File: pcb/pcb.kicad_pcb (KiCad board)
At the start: 2 copper layers, 347.8 x 133.5 mm, 250 parts, among them J1 USB_C_Receptacle_USB2.0_16P, SW1 SW_Push, U1 USBLC6-2SC6, U2 XC6206PxxxMR, U3 STM32F072CBTx

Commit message: Matrix ready
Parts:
- moved D10 9.62 mm to (226.1, 47.0), turned to 90 degrees
- moved D13 9.62 mm to (283.2, 47.0), turned to 90 degrees
- moved D14 9.62 mm to (302.3, 47.0), turned to 90 degrees
- moved D5 9.62 mm to (130.8, 47.0), turned to 90 degrees
- moved D7 9.62 mm to (168.9, 47.0), turned to 90 degrees
- moved D8 9.62 mm to (188.0, 47.0), turned to 90 degrees
- moved D9 9.62 mm to (207.0, 47.0), turned to 90 degrees
- moved D4 9.62 mm to (111.8, 47.0), turned to 90 degrees
- moved D11 9.62 mm to (245.1, 47.0), turned to 90 degrees
- moved D6 9.62 mm to (149.9, 47.0), turned to 90 degrees
- moved D12 9.62 mm to (264.2, 47.0), turned to 90 degrees
- moved D45 9.24 mm to (326.1, 74.0)
- moved D46 9.24 mm to (345.1, 74.0)
- moved D47 9.24 mm to (364.2, 74.0)
- moved D17 9.21 mm to (73.7, 55.0)
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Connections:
- U3 pad 15: Co17 -> Co4
- U3 pad 45: Co4 -> Co17
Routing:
- net Ro1: track 0.00 -> 266.7 mm
- net Ro0: track 38.1 -> 249.9 mm
- net Ro2: track 271.5 -> 328.6 mm
- net Co17: track 66.7 -> 108.6 mm
- net Net-(D47-A): track 0.00 -> 6.80 mm
- net Net-(D46-A): track 0.00 -> 6.80 mm
- net Net-(D45-A): track 0.00 -> 6.80 mm
- net Net-(D29-A): track 0.00 -> 6.74 mm
- net Net-(D28-A): track 0.00 -> 6.74 mm
- net Net-(D27-A): track 0.00 -> 6.74 mm
- net Net-(D26-A): track 0.00 -> 6.74 mm
- net Net-(D25-A): track 0.00 -> 6.74 mm
- net Net-(D24-A): track 0.00 -> 6.74 mm
- net Net-(D23-A): track 0.00 -> 6.74 mm
- net Net-(D22-A): track 0.00 -> 6.74 mm
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
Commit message: Change generic diodes to SOD-123
50% done
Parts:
- D1, D10, D100, D101, D102, D103, D104, D105, D106, D107, D108, D109, D11, D110, D111, D12, D13, D14, D15, D16, D17, D18, D19, D2, D20, D21, D22, D23, D24, D25, D26, D27, D28, D29, D3, D30, D31, D32, D33, D34, D35, D36, D37, D38, D39, D4, D40, D41, D42, D43, D44, D45, D46, D47, D48, D49, D5, D50, D51, D52, D53, D54, D55, D56, D57, D58, D59, D6, D60, D61, D62, D63, D64, D65, D66, D67, D68, D69, D7, D70, D71, D72, D73, D74, D75, D76, D77, D78, D79, D8, D80, D81, D82, D83, D84, D85, D86, D87, D88, D89, D9, D90, D91, D92, D93, D94, D95, D96, D97, D98, D99: footprint Diode_SMD:D_0402_1005Metric -> Diode_SMD:D_SOD-123
- moved D43 2.38 mm to (283.8, 72.4)
- moved D48 2.34 mm to (36.2, 91.4)
- moved D27 2.09 mm to (262.9, 53.3)
- moved D19 2.09 mm to (110.5, 53.3)
- moved D20 2.09 mm to (129.5, 53.3)
- moved D21 2.09 mm to (148.6, 53.3)
- moved D22 2.09 mm to (167.6, 53.3)
- moved D23 2.09 mm to (186.7, 53.3)
- moved D25 2.09 mm to (224.8, 53.3)
- moved D26 2.09 mm to (243.8, 53.3)
- moved D15 2.09 mm to (34.3, 53.3)
- moved D16 2.09 mm to (53.3, 53.3)
- moved D17 2.09 mm to (72.4, 53.3)
- moved D18 2.09 mm to (91.4, 53.3)
- moved D24 2.09 mm to (205.7, 53.3)
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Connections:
- U3 pad 14: Co16 -> Co5
- U3 pad 46: Co5 -> Co16
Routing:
- net Co16: track 76.2 -> 107.4 mm, vias 0 -> 1
- net Co17: track 108.6 -> 117.1 mm
- net Ro3: track 330.0 -> 331.6 mm
- net Ro0: track 249.9 -> 248.4 mm
- net Net-(D43-A): track 6.80 -> 7.96 mm
- net Net-(D48-A): track 6.84 -> 7.96 mm
- net Net-(D27-A): track 6.74 -> 7.77 mm
- net Net-(D26-A): track 6.74 -> 7.77 mm
- net Net-(D25-A): track 6.74 -> 7.77 mm
- net Net-(D23-A): track 6.74 -> 7.77 mm
- net Net-(D22-A): track 6.74 -> 7.77 mm
- net Net-(D21-A): track 6.74 -> 7.77 mm
- net Net-(D20-A): track 6.74 -> 7.77 mm
- net Net-(D19-A): track 6.74 -> 7.77 mm
- net Net-(D15-A): track 6.74 -> 7.77 mm
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
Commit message: finished diodes and finished top MCU datalines
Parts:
- moved D66 2.31 mm to (36.2, 110.5)
- moved D104 2.28 mm to (198.1, 148.6)
- moved D82 2.28 mm to (36.2, 129.5)
- moved D106 2.24 mm to (245.7, 148.6)
- moved D100 2.24 mm to (36.2, 148.6)
- moved D102 2.24 mm to (83.8, 148.6)
- moved D103 2.24 mm to (141.0, 148.6)
- moved D99 1.96 mm to (363.9, 139.1)
- moved D105 1.62 mm to (222.9, 148.6)
- moved D101 1.62 mm to (61.0, 148.6)
- moved D73 1.54 mm to (173.4, 110.5)
- moved D67 1.54 mm to (59.1, 110.5)
- moved D68 1.54 mm to (78.1, 110.5)
- moved D69 1.54 mm to (97.2, 110.5)
- moved D70 1.54 mm to (116.2, 110.5)
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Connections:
- U3 pad 15: Co4 -> Co8
- U3 pad 17: Co0 -> Co11
- U3 pad 2: Ro0 -> Co9
- U3 pad 25: Co8 -> Co4
- U3 pad 26: Co9 -> Co3
- U3 pad 27: Co10 -> Co2
- U3 pad 28: Co11 -> Co1
- U3 pad 29: Co1 -> Co0
- U3 pad 3: Ro1 -> Co10
- U3 pad 30: Co2 -> Ro1
- U3 pad 31: Co3 -> Ro0
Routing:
- net Co0: track 96.2 -> 402.4 mm, vias 0 -> 1
- net Co1: track 117.3 -> 403.9 mm, vias 0 -> 1
- net Co2: track 119.2 -> 386.1 mm, vias 0 -> 1
- net Co3: track 97.2 -> 344.4 mm, vias 0 -> 1
- net Co4: track 97.2 -> 324.6 mm, vias 0 -> 1
- net Ro1: track 266.7 -> 302.9 mm
- net Ro0: track 248.4 -> 283.3 mm
- net Ro4: track 307.2 -> 311.3 mm
- net Ro6: track 307.2 -> 308.6 mm
- net Ro5: track 330.4 -> 331.6 mm
- net Net-(D66-A): track 6.89 -> 7.96 mm
- net Net-(D82-A): track 6.94 -> 7.96 mm
- net Net-(D104-A): track 7.01 -> 8.03 mm
- net Net-(D103-A): track 7.00 -> 7.97 mm
- net Net-(D106-A): track 6.99 -> 7.96 mm
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
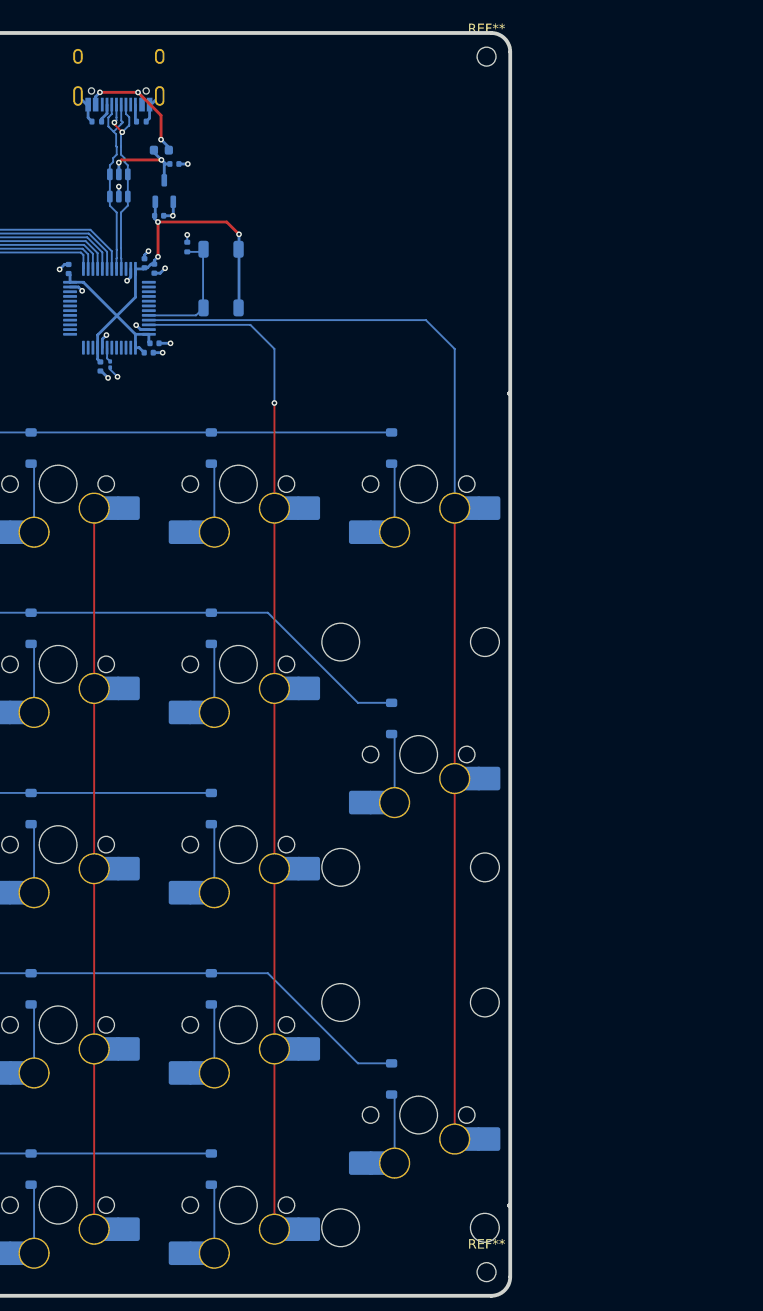
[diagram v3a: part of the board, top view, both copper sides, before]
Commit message: Add some LSCPCB footprints
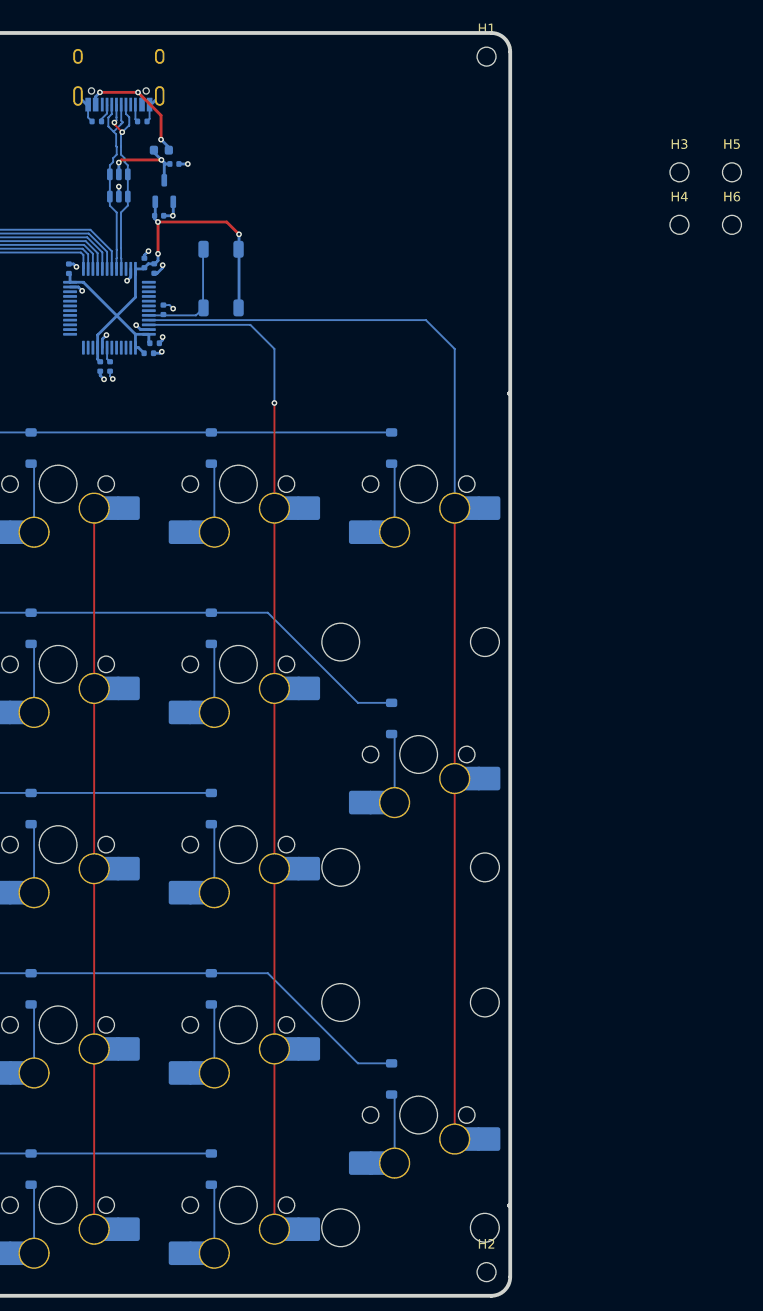
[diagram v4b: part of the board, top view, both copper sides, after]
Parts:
- removed the REF** at (373.9, 159.5)
- removed the REF** at (373.9, 31.0)
- added H1: MountingHole, MountingHole:MountingHole_2mm, F.Cu at (373.9, 31.0)
- added H2: MountingHole, MountingHole:MountingHole_2mm, F.Cu at (373.9, 159.5)
- added H3: MountingHole, MountingHole:MountingHole_2mm, F.Cu at (394.3, 43.2)
- added H4: MountingHole, MountingHole:MountingHole_2mm, F.Cu at (394.3, 48.8)
- added H5: MountingHole, MountingHole:MountingHole_2mm, F.Cu at (399.8, 43.2)
- added H6: MountingHole, MountingHole:MountingHole_2mm, F.Cu at (399.8, 48.8)
- C1, C2, C3, C4, C5: value 100n -> 100nF; footprint Capacitor_SMD:C_0402_1005Metric -> PCM_JLCPCB:C_0402
- C6: value 10u -> 10uF; footprint Capacitor_SMD:C_0402_1005Metric -> PCM_JLCPCB:C_0402
- C7: value 100n -> 100nF; footprint Capacitor_SMD:C_0201_0603Metric -> PCM_JLCPCB:C_0402
- R1, R2: value 5k1 -> 5.1kΩ; footprint Resistor_SMD:R_0402_1005Metric -> PCM_JLCPCB:R_0402
- R3: value 10k -> 10kΩ; footprint Resistor_SMD:R_0402_1005Metric -> PCM_JLCPCB:R_0402
- moved R3 7.09 mm to (339.7, 57.8)
- moved C7 0.21 mm to (334.1, 63.8)
- moved R2 0.10 mm to (337.5, 37.9)
- moved C1 0.06 mm to (338.2, 62.4), turned to 180 degrees
- turned C2 to -90 degrees
- turned C5 to -90 degrees
- turned C4 to 90 degrees
- turned C3 to 180 degrees
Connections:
- C1 pad 1: +3.3V -> GND
- C1 pad 2: GND -> +3.3V
- C2 pad 1: +3.3V -> GND
- C2 pad 2: GND -> +3.3V
- C3 pad 1: +3.3V -> GND
- C3 pad 2: GND -> +3.3V
- C4 pad 1: +3.3V -> GND
- C4 pad 2: GND -> +3.3V
- C5 pad 1: +3.3V -> GND
- C5 pad 2: GND -> +3.3V
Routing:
- net BOOT0: track 14.2 -> 12.9 mm

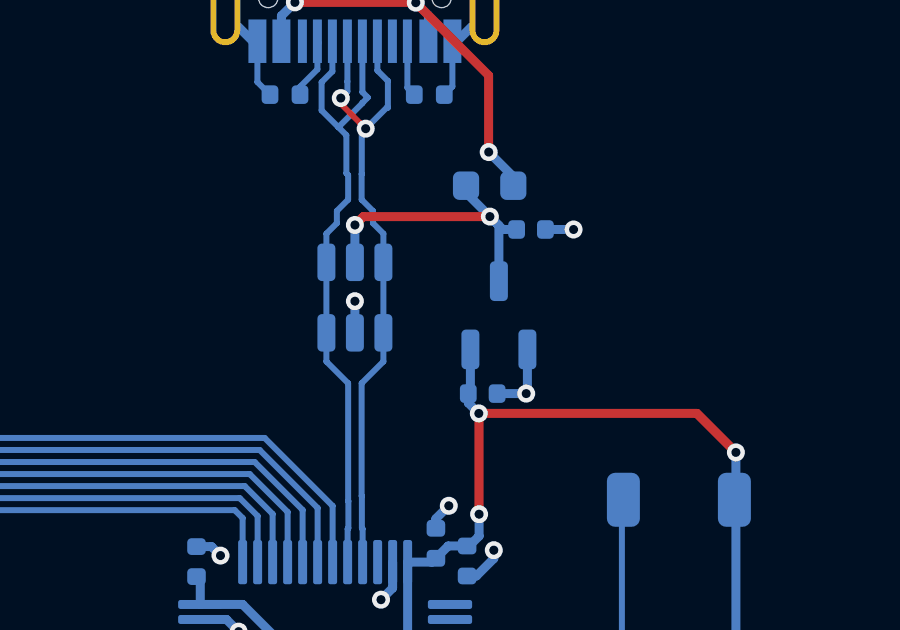
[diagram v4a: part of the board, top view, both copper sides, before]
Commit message: Replace some more with LSCPCB library
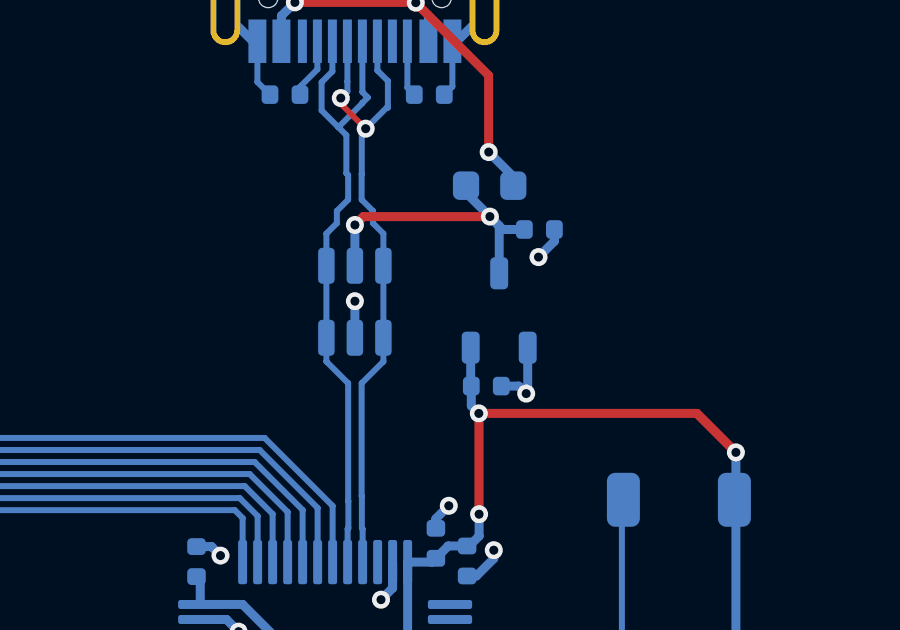
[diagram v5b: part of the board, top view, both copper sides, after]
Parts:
- C8, C9: value 1u -> 1uF; footprint Capacitor_SMD:C_0402_1005Metric -> PCM_JLCPCB:C_0402
- D1, D10, D100, D101, D102, D103, D104, D105, D106, D107, D108, D109, D11, D110, D111, D12, D13, D14, D15, D16, D17, D18, D19, D2, D20, D21, D22, D23, D24, D25, D26, D27, D28, D29, D3, D30, D31, D32, D33, D34, D35, D36, D37, D38, D39, D4, D40, D41, D42, D43, D44, D45, D46, D47, D48, D49, D5, D50, D51, D52, D53, D54, D55, D56, D57, D58, D59, D6, D60, D61, D62, D63, D64, D65, D66, D67, D68, D69, D7, D70, D71, D72, D73, D74, D75, D76, D77, D78, D79, D8, D80, D81, D82, D83, D84, D85, D86, D87, D88, D89, D9, D90, D91, D92, D93, D94, D95, D96, D97, D98, D99: value D -> Switching,1N4148W,(2)
- U1: value USBLC6-2SC6 -> SRV05-4_C7420376; footprint PCM_marbastlib-various:SOT-23-6-routable -> PCM_JLCPCB:SOT-23-6_L2.9-W1.6-P0.95-LS2.8-BL-1
- U2: value XC6206PxxxMR -> XC6206P332MR; footprint Package_TO_SOT_SMD:SOT-23-3 -> PCM_JLCPCB:SOT-23-3_L2.9-W1.6-P1.90-LS2.8-BR
- moved C8 0.28 mm to (341.2, 42.4)
- moved C9 0.28 mm to (339.4, 47.6)
- moved U2 0.16 mm to (339.8, 45.1), turned to -90 degrees
- moved U1 0.14 mm to (335.0, 44.8), turned to 180 degrees

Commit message: matrix connected
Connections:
- U3 pad 10: Co12 -> Ro3
- U3 pad 11: Co13 -> Ro2
- U3 pad 12: Co14 -> Co15
- U3 pad 13: Co15 -> Co14
- U3 pad 14: Co5 -> Co13
- U3 pad 15: Co8 -> Co12
- U3 pad 16: Ro6 -> Co11
- U3 pad 17: Co11 -> Co10
- U3 pad 18: Ro3 -> Co9
- U3 pad 19: Ro4 -> Co8
- U3 pad 2: Co9 -> Ro6
- U3 pad 20: Ro5 -> Co7
- U3 pad 22: Co7 -> Co5
- U3 pad 3: Co10 -> Ro5
- U3 pad 4: Ro2 -> Ro4
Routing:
- net Co5: track 119.2 -> 318.6 mm, vias 0 -> 1
- net Co6: track 97.2 -> 277.5 mm, vias 0 -> 1
- net Co7: track 97.2 -> 258.4 mm, vias 0 -> 1
- net Co8: track 119.2 -> 261.3 mm, vias 0 -> 1
- net Co9: track 97.2 -> 220.2 mm, vias 0 -> 1
- net Co10: track 119.2 -> 223.1 mm, vias 0 -> 1
- net Ro6: track 308.6 -> 394.8 mm, vias 0 -> 2
- net Co11: track 117.3 -> 202.1 mm, vias 0 -> 1
- net Ro5: track 331.6 -> 398.5 mm, vias 0 -> 2
- net Co12: track 124.2 -> 189.8 mm, vias 0 -> 1
- net Co13: track 117.0 -> 173.2 mm, vias 0 -> 1
- net Ro4: track 311.3 -> 358.9 mm, vias 0 -> 2
- net Co14: track 116.3 -> 153.5 mm, vias 0 -> 1
- net Ro3: track 331.6 -> 361.1 mm, vias 0 -> 2
- net Co15: track 76.2 -> 93.6 mm, vias 0 -> 1
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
